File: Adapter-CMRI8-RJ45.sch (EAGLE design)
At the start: 17 parts, among them CON1 CONNECTOR-M033.5MM-LOCK, J1 RJ45, M1 MOUNTINGHOLE, M2 MOUNTINGHOLE

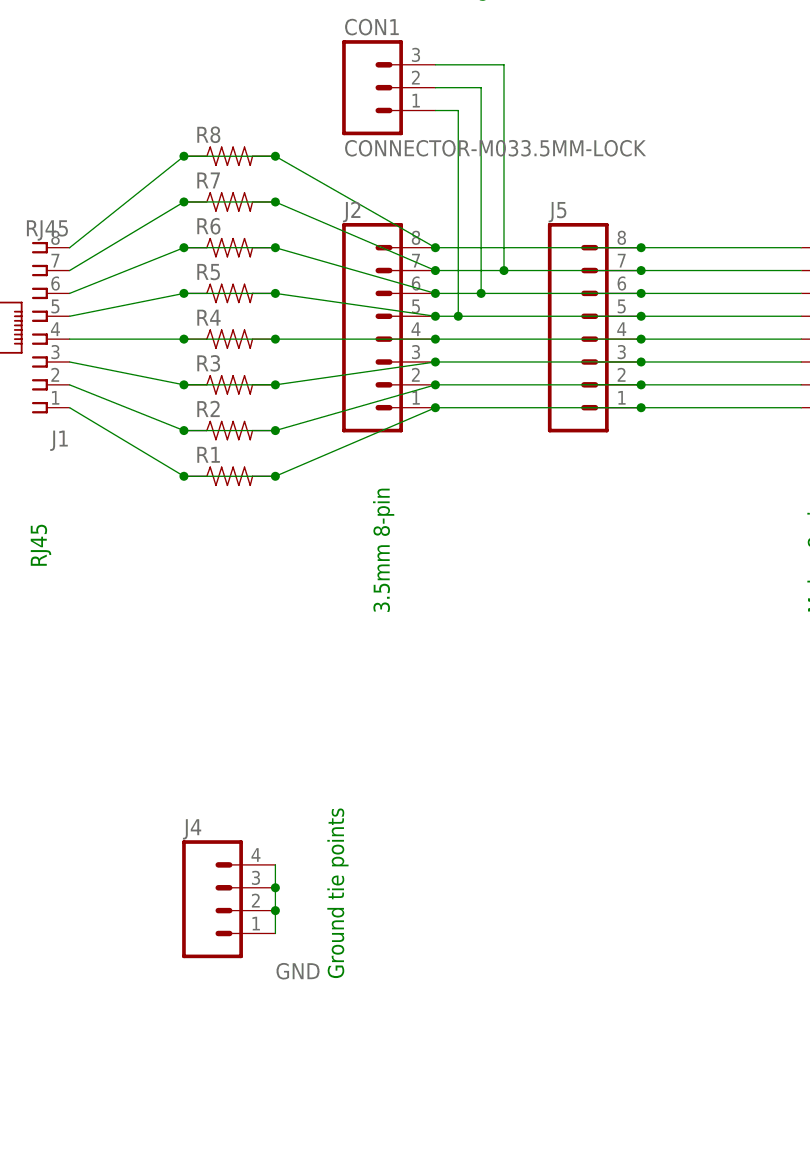
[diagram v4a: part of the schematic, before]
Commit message: added values for connectors
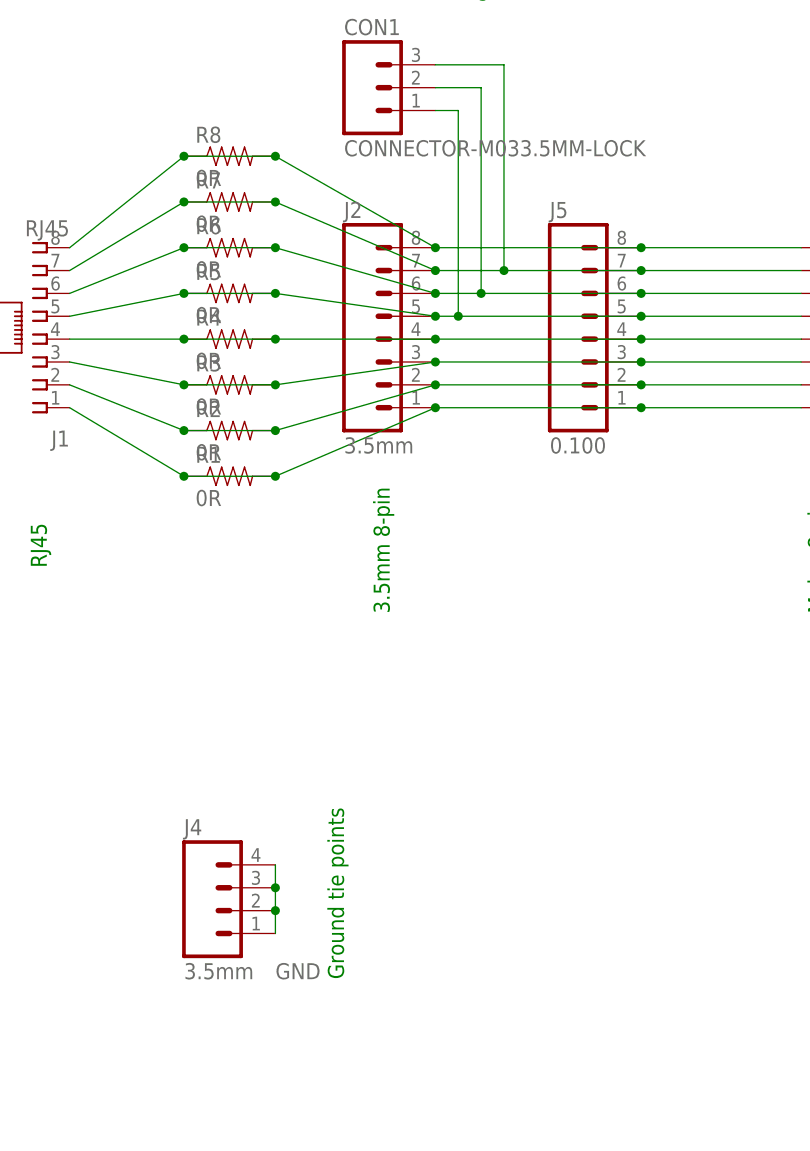
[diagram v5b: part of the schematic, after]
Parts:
- J2, J4: value (none) -> 3.5mm
- J5: value (none) -> 0.100
- R1, R2, R3, R4, R5, R6, R7, R8: value (none) -> 0R
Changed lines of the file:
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@@
 <grid distance="100" unitdist="mil" unit="mil" style="dots" multiple="1" display="yes" altdistance="50" altunitdist="mil" altunit="mil"/>
 <layers>
-<layer number="1" name="Top" color="4" fill="1" visible="yes" active="no"/>
-<layer number="2" name="Route2" color="1" fill="3" visible="yes" active="no"/>
-<layer number="3" name="Route3" color="4" fill="3" visible="yes" active="no"/>
-<layer number="14" name="Route14" color="1" fill="6" visible="yes" active="no"/>
-<layer number="15" name="Route15" color="4" fill="6" visible="yes" active="no"/>
-<layer number="16" name="Bottom" color="1" fill="1" visible="yes" active="no"/>
-<layer number="17" name="Pads" color="2" fill="1" visible="yes" active="no"/>
-<layer number="18" name="Vias" color="2" fill="1" visible="yes" active="no"/>
-<layer number="19" name="Unrouted" color="6" fill="1" visible="yes" active="no"/>
-<layer number="20" name="Dimension" color="15" fill="1" visible="yes" active="no"/>
-<layer number="21" name="tPlace" color="5" fill="1" visible="yes" active="no"/>
-<layer number="22" name="bPlace" color="7" fill="1" visible="yes" active="no"/>
-<layer number="23" name="tOrigins" color="15" fill="1" visible="yes" active="no"/>
-<layer number="24" name="bOrigins" color="15" fill="1" visible="yes" active="no"/>
-<layer number="25" name="tNames" color="7" fill="1" visible="yes" active="no"/>
-<layer number="26" name="bNames" color="7" fill="1" visible="yes" active="no"/>
-<layer number="27" name="tValues" color="7" fill="1" visible="yes" active="no"/>
-<layer number="28" name="bValues" color="7" fill="1" visible="yes" active="no"/>
+<layer number="1" name="Top" color="4" fill="1" visible="no" active="no"/>
+<layer number="2" name="Route2" color="1" fill="3" visible="no" active="no"/>
+<layer number="3" name="Route3" color="4" fill="3" visible="no" active="no"/>
+<layer number="14" name="Route14" color="1" fill="6" visible="no" active="no"/>
+<layer number="15" name="Route15" color="4" fill="6" visible="no" active="no"/>
+<layer number="16" name="Bottom" color="1" fill="1" visible="no" active="no"/>
+<layer number="17" name="Pads" color="2" fill="1" visible="no" active="no"/>
+<layer number="18" name="Vias" color="2" fill="1" visible="no" active="no"/>
+<layer number="19" name="Unrouted" color="6" fill="1" visible="no" active="no"/>
+<layer number="20" name="Dimension" color="15" fill="1" visible="no" active="no"/>
+<layer number="21" name="tPlace" color="5" fill="1" visible="no" active="no"/>
+<layer number="22" name="bPlace" color="7" fill="1" visible="no" active="no"/>
+<layer number="23" name="tOrigins" color="15" fill="1" visible="no" active="no"/>
+<layer number="24" name="bOrigins" color="15" fill="1" visible="no" active="no"/>
+<layer number="25" name="tNames" color="7" fill="1" visible="no" active="no"/>
+<layer number="26" name="bNames" color="7" fill="1" visible="no" active="no"/>
+<layer number="27" name="tValues" color="7" fill="1" visible="no" active="no"/>
+<layer number="28" name="bValues" color="7" fill="1" visible="no" active="no"/>
 <layer number="29" name="tStop" color="7" fill="3" visible="no" active="no"/>
 <layer number="30" name="bStop" color="7" fill="6" visible="no" active="no"/>
@@
 <layer number="35" name="tGlue" color="7" fill="4" visible="no" active="no"/>
 <layer number="36" name="bGlue" color="7" fill="5" visible="no" active="no"/>
-<layer number="37" name="tTest" color="7" fill="1" visible="yes" active="no"/>
-<layer number="38" name="bTest" color="7" fill="1" visible="yes" active="no"/>
+<layer number="37" name="tTest" color="7" fill="1" visible="no" active="no"/>
+<layer number="38" name="bTest" color="7" fill="1" visible="no" active="no"/>
 <layer number="39" name="tKeepout" color="4" fill="11" visible="no" active="no"/>
 <layer number="40" name="bKeepout" color="1" fill="11" visible="no" active="no"/>
@@
 <layer number="44" name="Drills" color="7" fill="1" visible="no" active="no"/>
 <layer number="45" name="Holes" color="7" fill="1" visible="no" active="no"/>
-<layer number="46" name="Milling" color="3" fill="1" visible="yes" active="no"/>
-<layer number="47" name="Measures" color="7" fill="1" visible="yes" active="no"/>
-<layer number="48" name="Document" color="7" fill="1" visible="yes" active="no"/>
-<layer number="49" name="Reference" color="7" fill="1" visible="yes" active="no"/>
-<layer number="50" name="dxf" color="7" fill="1" visible="yes" active="no"/>
-<layer number="51" name="tDocu" color="51" fill="1" visible="yes" active="no"/>
-<layer number="52" name="bDocu" color="15" fill="1" visible="yes" active="no"/>
-<layer number="53" name="tGND_GNDA" color="7" fill="9" visible="yes" active="no"/>
-<layer number="54" name="bGND_GNDA" color="1" fill="9" visible="yes" active="no"/>
-<layer number="56" name="wert" color="49" fill="1" visible="yes" active="no"/>
-<layer number="57" name="tCAD" color="7" fill="1" visible="yes" active="no"/>
-<layer number="59" name="tCarbon" color="7" fill="1" visible="yes" active="no"/>
-<layer number="60" name="bCarbon" color="7" fill="1" visible="yes" active="no"/>
+<layer number="46" name="Milling" color="3" fill="1" visible="no" active="no"/>
+<layer number="47" name="Measures" color="7" fill="1" visible="no" active="no"/>
+<layer number="48" name="Document" color="7" fill="1" visible="no" active="no"/>
+<layer number="49" name="Reference" color="7" fill="1" visible="no" active="no"/>
+<layer number="50" name="dxf" color="7" fill="1" visible="no" active="no"/>
+<layer number="51" name="tDocu" color="51" fill="1" visible="no" active="no"/>
+<layer number="52" name="bDocu" color="15" fill="1" visible="no" active="no"/>
+<layer number="53" name="tGND_GNDA" color="7" fill="9" visible="no" active="no"/>
+<layer number="54" name="bGND_GNDA" color="1" fill="9" visible="no" active="no"/>
+<layer number="56" name="wert" color="49" fill="1" visible="no" active="no"/>
+<layer number="57" name="tCAD" color="7" fill="1" visible="no" active="no"/>
+<layer number="59" name="tCarbon" color="7" fill="1" visible="no" active="no"/>
+<layer number="60" name="bCarbon" color="7" fill="1" visible="no" active="no"/>
 <layer number="90" name="Modules" color="5" fill="1" visible="yes" active="yes"/>
 <layer number="91" name="Nets" color="2" fill="1" visible="yes" active="yes"/>
@@
 <part name="FRAME1" library="SparkFun" deviceset="FRAME-LETTER" device=""/>
 <part name="J3" library="SPCoast" deviceset="KK-156-8" device="F"/>
-<part name="J2" library="SPCoast" deviceset="CONNECTOR-M08" device="3.5MM-8"/>
+<part name="J2" library="SPCoast" deviceset="CONNECTOR-M08" device="3.5MM-8" value="3.5mm"/>
 <part name="U$1" library="SPCoast" deviceset="DOC-OSHW-LOGO-" device="L" value="DOC-OSHW-LOGO-L"/>
 <part name="J1" library="SPCoast" deviceset="CONNECTOR-RJ45" device="-FRONT" value="RJ45"/>
-<part name="J4" library="SPCoast" deviceset="CONNECTOR-M04" device="SCREW_LOCK"/>
+<part name="J4" library="SPCoast" deviceset="CONNECTOR-M04" device="SCREW_LOCK" value="3.5mm"/>
 <part name="M1" library="SPCoast" deviceset="MOUNTINGHOLE" device=""/>
 <part name="M2" library="SPCoast" deviceset="MOUNTINGHOLE" device=""/>
-<part name="J5" library="SPCoast" deviceset="CONNECTOR-M08" device="LOCK"/>
-<part name="R1" library="SPCoast" deviceset="R*" device="PTH04"/>
-<part name="R2" library="SPCoast" deviceset="R*" device="PTH04"/>
-<part name="R3" library="SPCoast" deviceset="R*" device="PTH04"/>
-<part name="R4" library="SPCoast" deviceset="R*" device="PTH04"/>
-<part name="R5" library="SPCoast" deviceset="R*" device="PTH04"/>
-<part name="R6" library="SPCoast" deviceset="R*" device="PTH04"/>
-<part name="R7" library="SPCoast" deviceset="R*" device="PTH04"/>
-<part name="R8" library="SPCoast" deviceset="R*" device="PTH04"/>
+<part name="J5" library="SPCoast" deviceset="CONNECTOR-M08" device="LOCK" value="0.100"/>
+<part name="R1" library="SPCoast" deviceset="R*" device="PTH04" value="0R"/>
+<part name="R2" library="SPCoast" deviceset="R*" device="PTH04" value="0R"/>
+<part name="R3" library="SPCoast" deviceset="R*" device="PTH04" value="0R"/>
+<part name="R4" library="SPCoast" deviceset="R*" device="PTH04" value="0R"/>
+<part name="R5" library="SPCoast" deviceset="R*" device="PTH04" value="0R"/>
+<part name="R6" library="SPCoast" deviceset="R*" device="PTH04" value="0R"/>
+<part name="R7" library="SPCoast" deviceset="R*" device="PTH04" value="0R"/>
+<part name="R8" library="SPCoast" deviceset="R*" device="PTH04" value="0R"/>
 <part name="CON1" library="SPCoast" deviceset="CONNECTOR-M03" device="3.5MM-LOCK"/>
 </parts>

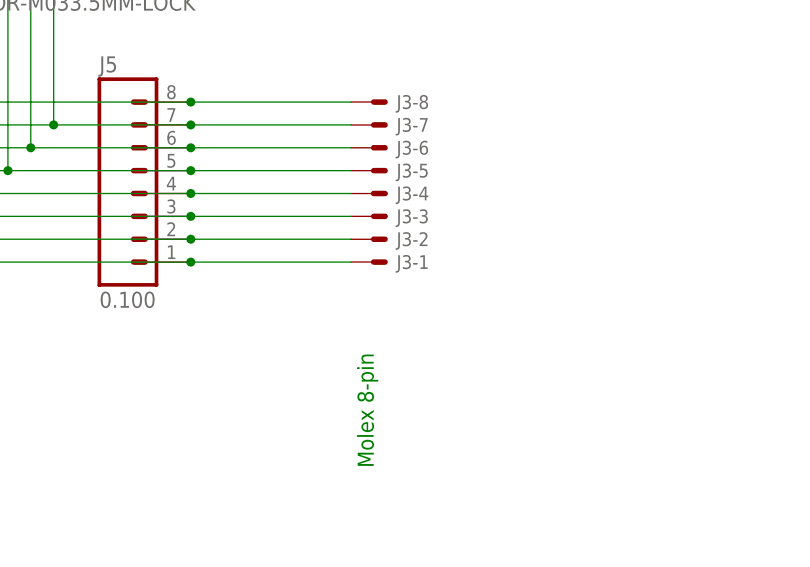
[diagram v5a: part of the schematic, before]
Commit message: added values for connectors
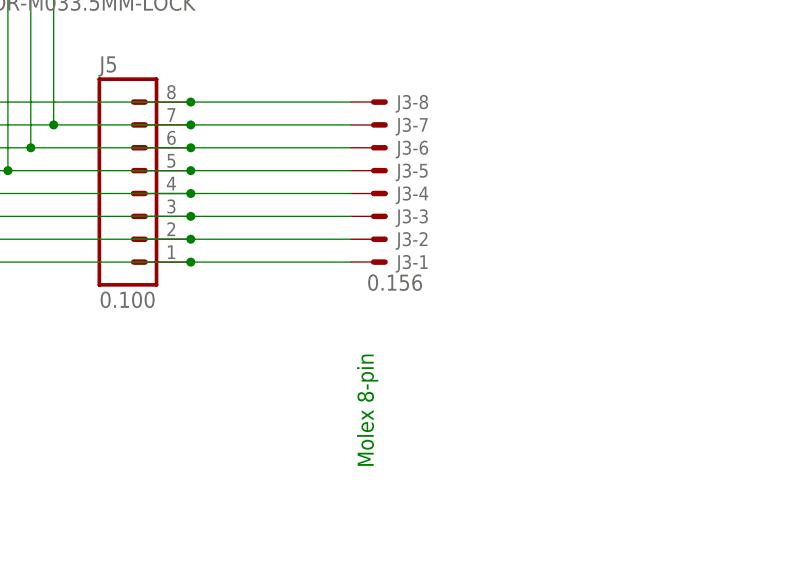
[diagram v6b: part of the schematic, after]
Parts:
- J3: value (none) -> 0.156
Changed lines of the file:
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@@
 <parts>
 <part name="FRAME1" library="SparkFun" deviceset="FRAME-LETTER" device=""/>
-<part name="J3" library="SPCoast" deviceset="KK-156-8" device="F"/>
+<part name="J3" library="SPCoast" deviceset="KK-156-8" device="F" value="0.156"/>
 <part name="J2" library="SPCoast" deviceset="CONNECTOR-M08" device="3.5MM-8" value="3.5mm"/>
 <part name="U$1" library="SPCoast" deviceset="DOC-OSHW-LOGO-" device="L" value="DOC-OSHW-LOGO-L"/>

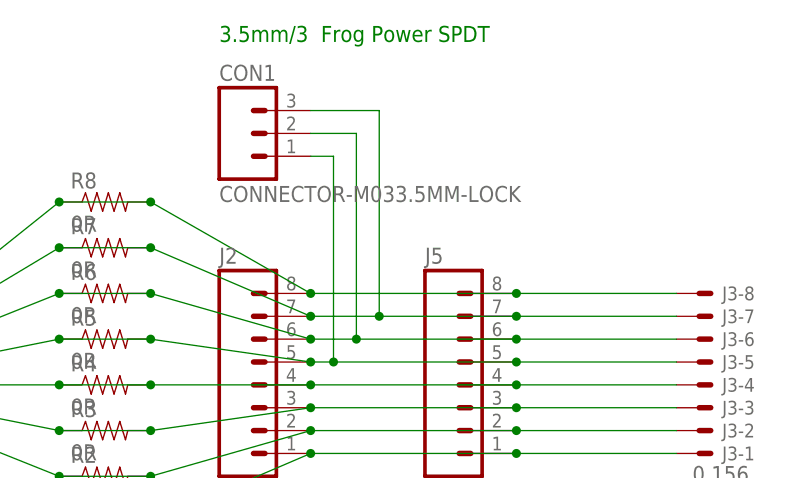
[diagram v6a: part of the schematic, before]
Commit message: normalized values
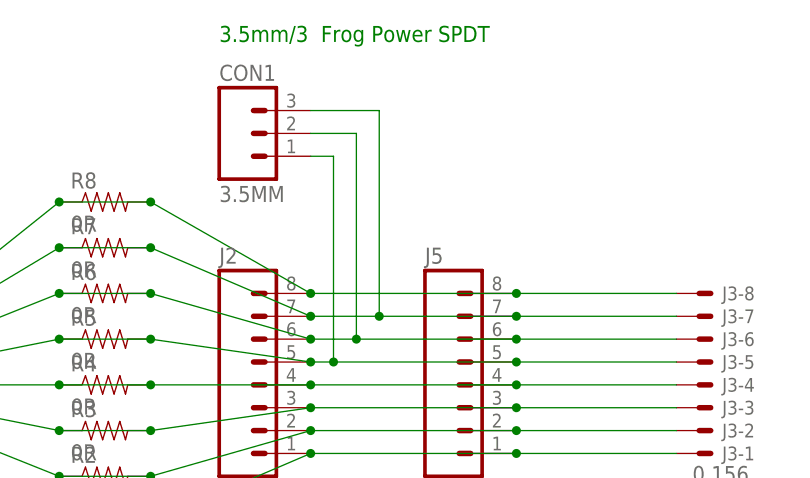
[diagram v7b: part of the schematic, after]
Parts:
- CON1: value CONNECTOR-M033.5MM-LOCK -> 3.5MM
- U$1: value DOC-OSHW-LOGO-L -> OSHW
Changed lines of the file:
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@@
 <part name="J3" library="SPCoast" deviceset="KK-156-8" device="F" value="0.156"/>
 <part name="J2" library="SPCoast" deviceset="CONNECTOR-M08" device="3.5MM-8" value="3.5mm"/>
-<part name="U$1" library="SPCoast" deviceset="DOC-OSHW-LOGO-" device="L" value="DOC-OSHW-LOGO-L"/>
+<part name="U$1" library="SPCoast" deviceset="DOC-OSHW-LOGO-" device="L" value="OSHW"/>
 <part name="J1" library="SPCoast" deviceset="CONNECTOR-RJ45" device="-FRONT" value="RJ45"/>
 <part name="J4" library="SPCoast" deviceset="CONNECTOR-M04" device="SCREW_LOCK" value="3.5mm"/>
@@
 <part name="R7" library="SPCoast" deviceset="R*" device="PTH04" value="0R"/>
 <part name="R8" library="SPCoast" deviceset="R*" device="PTH04" value="0R"/>
-<part name="CON1" library="SPCoast" deviceset="CONNECTOR-M03" device="3.5MM-LOCK"/>
+<part name="CON1" library="SPCoast" deviceset="CONNECTOR-M03" device="3.5MM-LOCK" value="3.5MM"/>
 </parts>
 <sheets>
